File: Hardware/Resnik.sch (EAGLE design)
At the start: 212 parts, among them IC1 ATMEGA1284M, J1 CONN_82.54_SCREW, J3 CONN_42.54_SCREW, J4 CONN_82.54_SCREW, Q1 DMG3404, Q2 DMG3404, Q3 FDN360P, Q4 2N7002, Q5 FDN360P, Q6 DMG3404, Q7 2N7002, Q8 2N7002, U1 TLV61220DBV, U10 TPS22917DBV, U11 SN74AUP1G04YFP, U12 SN74AUP1G04YFP, U13 SN74AUP1G04YFP, U14 SN74AUP2G08DQE, U15 SN74AUP2G08DQE, U16 SN74AUP2G08DQE, U17 MIC2544MSOP, U18 MIC2544MSOP, U19 MIC2544MSOP, U2 TPS62822DLC, U20 MIC2544MSOP, U21 TPS22917DBV, U22 TPS22917DBV, U23 FT231X-Q, U24 SN74LVC1G3157DRL, U25 SN74AUP3G34DCU, U26 TXS0102DQM, U27 TXS0104RGY, U28 TCA9406DCU, U29 TXS0104RGY, U3 TPS61032RSA, U30 MCP4726A2SOT-23, U31 BME280, U32 ADS1115, U33 ADS1115, U34 INA211DCK, U35 INA213DCK, U36 TCA9406DCU, U37 TLV3691DCK, U38 TS5A21366RSE, U39 MIC94094C6, U40 SN74AHC1G86DCK, U41 MCP23018QFN, U42 TXS0104RGY, U5 BQ2980RUG, U6 TPS2105, U7 LTC4412S6, U8 TPL5111DDC, U9 TPS79733

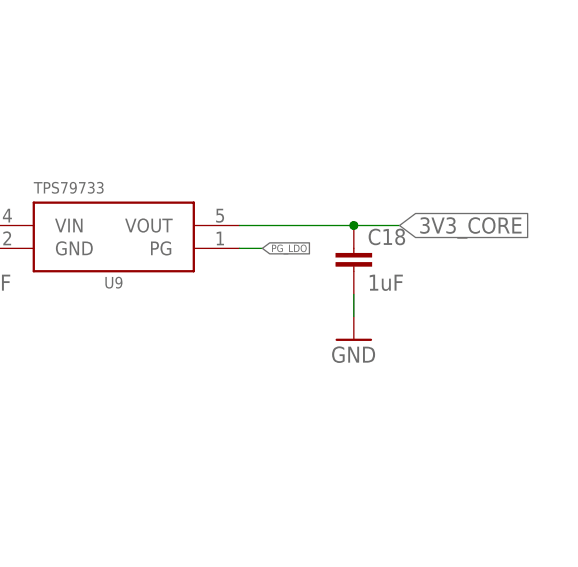
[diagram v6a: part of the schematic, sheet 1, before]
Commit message: Added Ref ID images, updated BoM for new parts, added pick and place
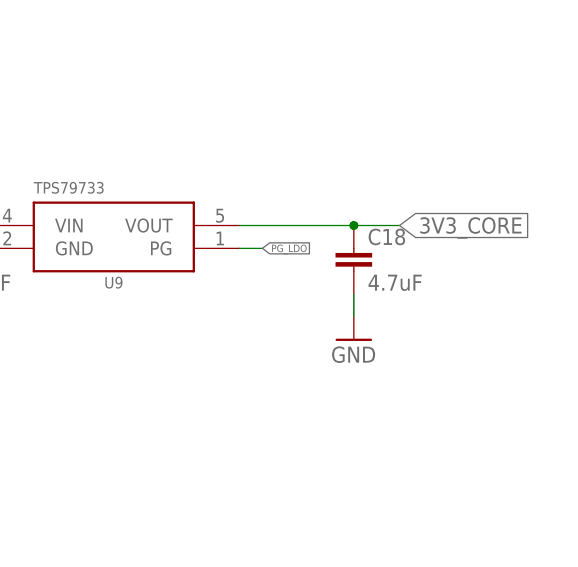
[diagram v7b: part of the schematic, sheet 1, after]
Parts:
- C18: value 1uF -> 4.7uF; device bschulz_passives:C-EU1UFC0603 -> bschulz_passives:C-EU4.7UFC0603
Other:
- note added: "J8"
- note added: "J9"
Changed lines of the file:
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@@
 <?xml version="1.0" encoding="utf-8"?>
 <!DOCTYPE eagle SYSTEM "eagle.dtd">
-<eagle version="9.2.1">
+<eagle version="9.4.2">
 <drawing>
 <settings>
@@
 <grid distance="0.1" unitdist="inch" unit="inch" style="lines" multiple="1" display="no" altdistance="0.01" altunitdist="inch" altunit="inch"/>
 <layers>
-<layer number="1" name="Top" color="4" fill="1" visible="yes" active="no"/>
-<layer number="2" name="Route2" color="16" fill="1" visible="yes" active="no"/>
-<layer number="3" name="Route3" color="17" fill="1" visible="yes" active="no"/>
-<layer number="4" name="Route4" color="18" fill="1" visible="yes" active="no"/>
-<layer number="5" name="Route5" color="19" fill="1" visible="yes" active="no"/>
-<layer number="6" name="Route6" color="25" fill="1" visible="yes" active="no"/>
-<layer number="7" name="Route7" color="26" fill="1" visible="yes" active="no"/>
-<layer number="8" name="Route8" color="27" fill="1" visible="yes" active="no"/>
-<layer number="9" name="Route9" color="28" fill="1" visible="yes" active="no"/>
-<layer number="10" name="Route10" color="29" fill="1" visible="yes" active="no"/>
-<layer number="11" name="Route11" color="30" fill="1" visible="yes" active="no"/>
-<layer number="12" name="Route12" color="20" fill="1" visible="yes" active="no"/>
-<layer number="13" name="Route13" color="21" fill="1" visible="yes" active="no"/>
-<layer number="14" name="Route14" color="22" fill="1" visible="yes" active="no"/>
-<layer number="15" name="Route15" color="23" fill="1" visible="yes" active="no"/>
-<layer number="16" name="Bottom" color="1" fill="1" visible="yes" active="no"/>
-<layer number="17" name="Pads" color="2" fill="1" visible="yes" active="no"/>
-<layer number="18" name="Vias" color="2" fill="1" visible="yes" active="no"/>
-<layer number="19" name="Unrouted" color="6" fill="1" visible="yes" active="no"/>
-<layer number="20" name="Dimension" color="24" fill="1" visible="yes" active="no"/>
-<layer number="21" name="tPlace" color="7" fill="1" visible="yes" active="no"/>
-<layer number="22" name="bPlace" color="7" fill="1" visible="yes" active="no"/>
-<layer number="23" name="tOrigins" color="15" fill="1" visible="yes" active="no"/>
-<layer number="24" name="bOrigins" color="15" fill="1" visible="yes" active="no"/>
-<layer number="25" name="tNames" color="7" fill="1" visible="yes" active="no"/>
-<layer number="26" name="bNames" color="7" fill="1" visible="yes" active="no"/>
-<layer number="27" name="tValues" color="7" fill="1" visible="yes" active="no"/>
-<layer number="28" name="bValues" color="7" fill="1" visible="yes" active="no"/>
+<layer number="1" name="Top" color="4" fill="1" visible="no" active="no"/>
+<layer number="2" name="Route2" color="16" fill="1" visible="no" active="no"/>
+<layer number="3" name="Route3" color="17" fill="1" visible="no" active="no"/>
+<layer number="4" name="Route4" color="18" fill="1" visible="no" active="no"/>
+<layer number="5" name="Route5" color="19" fill="1" visible="no" active="no"/>
+<layer number="6" name="Route6" color="25" fill="1" visible="no" active="no"/>
+<layer number="7" name="Route7" color="26" fill="1" visible="no" active="no"/>
+<layer number="8" name="Route8" color="27" fill="1" visible="no" active="no"/>
+<layer number="9" name="Route9" color="28" fill="1" visible="no" active="no"/>
+<layer number="10" name="Route10" color="29" fill="1" visible="no" active="no"/>
+<layer number="11" name="Route11" color="30" fill="1" visible="no" active="no"/>
+<layer number="12" name="Route12" color="20" fill="1" visible="no" active="no"/>
+<layer number="13" name="Route13" color="21" fill="1" visible="no" active="no"/>
+<layer number="14" name="Route14" color="22" fill="1" visible="no" active="no"/>
+<layer number="15" name="Route15" color="23" fill="1" visible="no" active="no"/>
+<layer number="16" name="Bottom" color="1" fill="1" visible="no" active="no"/>
+<layer number="17" name="Pads" color="2" fill="1" visible="no" active="no"/>
+<layer number="18" name="Vias" color="2" fill="1" visible="no" active="no"/>
+<layer number="19" name="Unrouted" color="6" fill="1" visible="no" active="no"/>
+<layer number="20" name="Dimension" color="24" fill="1" visible="no" active="no"/>
+<layer number="21" name="tPlace" color="7" fill="1" visible="no" active="no"/>
+<layer number="22" name="bPlace" color="7" fill="1" visible="no" active="no"/>
+<layer number="23" name="tOrigins" color="15" fill="1" visible="no" active="no"/>
+<layer number="24" name="bOrigins" color="15" fill="1" visible="no" active="no"/>
+<layer number="25" name="tNames" color="7" fill="1" visible="no" active="no"/>
+<layer number="26" name="bNames" color="7" fill="1" visible="no" active="no"/>
+<layer number="27" name="tValues" color="7" fill="1" visible="no" active="no"/>
+<layer number="28" name="bValues" color="7" fill="1" visible="no" active="no"/>
 <layer number="29" name="tStop" color="7" fill="3" visible="no" active="no"/>
 <layer number="30" name="bStop" color="7" fill="6" visible="no" active="no"/>
@@
 <layer number="35" name="tGlue" color="7" fill="4" visible="no" active="no"/>
 <layer number="36" name="bGlue" color="7" fill="5" visible="no" active="no"/>
-<layer number="37" name="tTest" color="7" fill="1" visible="yes" active="no"/>
-<layer number="38" name="bTest" color="7" fill="1" visible="yes" active="no"/>
+<layer number="37" name="tTest" color="7" fill="1" visible="no" active="no"/>
+<layer number="38" name="bTest" color="7" fill="1" visible="no" active="no"/>
 <layer number="39" name="tKeepout" color="4" fill="11" visible="no" active="no"/>
 <layer number="40" name="bKeepout" color="1" fill="11" visible="no" active="no"/>
@@
 <layer number="44" name="Drills" color="7" fill="1" visible="no" active="no"/>
 <layer number="45" name="Holes" color="7" fill="1" visible="no" active="no"/>
-<layer number="46" name="Milling" color="3" fill="1" visible="yes" active="no"/>
-<layer number="47" name="Measures" color="7" fill="1" visible="yes" active="no"/>
-<layer number="48" name="Document" color="7" fill="1" visible="yes" active="no"/>
-<layer number="49" name="Reference" color="7" fill="1" visible="yes" active="no"/>
-<layer number="50" name="dxf" color="7" fill="1" visible="yes" active="no"/>
-<layer number="51" name="tDocu" color="7" fill="1" visible="yes" active="no"/>
-<layer number="52" name="bDocu" color="7" fill="1" visible="yes" active="no"/>
-<layer number="53" name="tGND_GNDA" color="7" fill="1" visible="yes" active="no"/>
-<layer number="54" name="bGND_GNDA" color="7" fill="1" visible="yes" active="no"/>
-<layer number="56" name="wert" color="7" fill="1" visible="yes" active="no"/>
-<layer number="57" name="tCAD" color="7" fill="1" visible="yes" active="no"/>
-<layer number="59" name="tCarbon" color="7" fill="1" visible="yes" active="no"/>
-<layer number="60" name="bCarbon" color="7" fill="1" visible="yes" active="no"/>
+<layer number="46" name="Milling" color="3" fill="1" visible="no" active="no"/>
+<layer number="47" name="Measures" color="7" fill="1" visible="no" active="no"/>
+<layer number="48" name="Document" color="7" fill="1" visible="no" active="no"/>
+<layer number="49" name="Reference" color="7" fill="1" visible="no" active="no"/>
+<layer number="50" name="dxf" color="7" fill="1" visible="no" active="no"/>
+<layer number="51" name="tDocu" color="7" fill="1" visible="no" active="no"/>
+<layer number="52" name="bDocu" color="7" fill="1" visible="no" active="no"/>
+<layer number="53" name="tGND_GNDA" color="7" fill="1" visible="no" active="no"/>
+<layer number="54" name="bGND_GNDA" color="7" fill="1" visible="no" active="no"/>
+<layer number="56" name="wert" color="7" fill="1" visible="no" active="no"/>
+<layer number="57" name="tCAD" color="7" fill="1" visible="no" active="no"/>
+<layer number="59" name="tCarbon" color="7" fill="1" visible="no" active="no"/>
+<layer number="60" name="bCarbon" color="7" fill="1" visible="no" active="no"/>
 <layer number="88" name="SimResults" color="9" fill="1" visible="yes" active="yes"/>
 <layer number="89" name="SimProbes" color="9" fill="1" visible="yes" active="yes"/>
@@
 <part name="C17" library="bschulz_passives" deviceset="C-EU" device="C0402" technology="0.1UF" value="0.1uF"/>
 <part name="GND26" library="supply1" library_urn="urn:adsk.eagle:library:371" deviceset="GND" device=""/>
-<part name="C18" library="bschulz_passives" deviceset="C-EU" device="C0603" technology="1UF" value="1uF"/>
+<part name="C18" library="bschulz_passives" deviceset="C-EU" device="C0603" technology="4.7UF" value="4.7uF"/>
 <part name="GND27" library="supply1" library_urn="urn:adsk.eagle:library:371" deviceset="GND" device=""/>
 <part name="U7" library="bschulz" deviceset="LTC4412" device="S6"/>
@@
 <text x="129.54" y="91.44" size="1.778" layer="91">ICSP</text>
 <text x="134.62" y="114.3" size="1.778" layer="91">Jump SDA channels together, prevents using occupied addresses on the external I2C port</text>
+<text x="111.76" y="66.04" size="1.778" layer="95">J8</text>
+<text x="152.4" y="66.04" size="1.778" layer="95">J9</text>
 </plain>
 <instances>

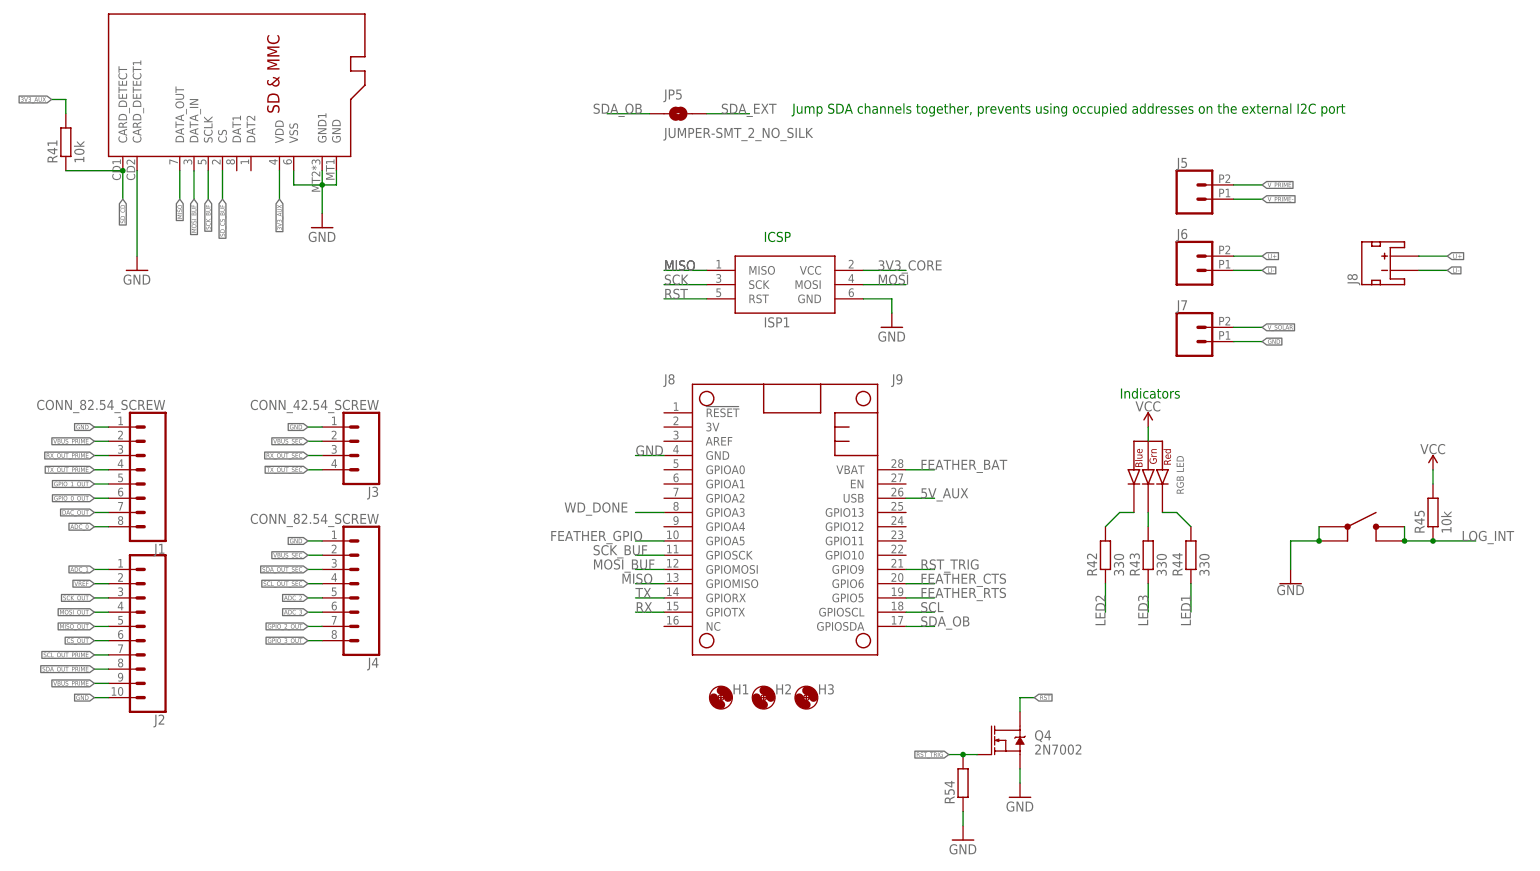
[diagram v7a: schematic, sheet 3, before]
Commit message: Added reference designators, cleanup
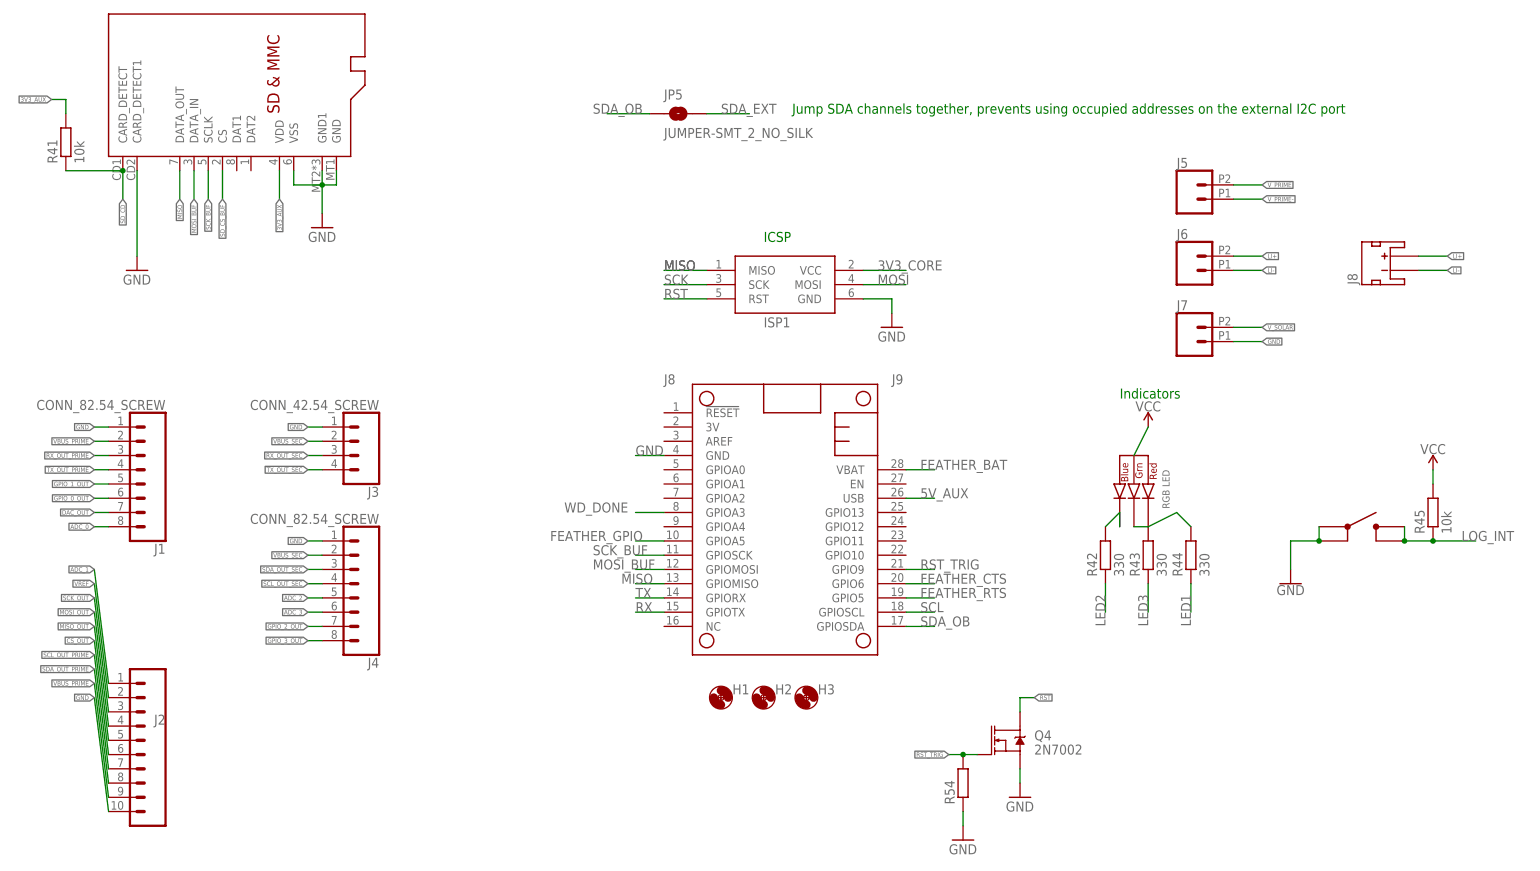
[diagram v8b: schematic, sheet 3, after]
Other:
- moved on the sheet: J2
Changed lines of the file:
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@@
 <wire x1="299.212" y1="109.22" x2="284.48" y2="109.22" width="0.1524" layer="91"/>
 <pinref part="D4" gate="G$1" pin="ANODE"/>
-<wire x1="299.212" y1="112.014" x2="299.212" y2="109.22" width="0.1524" layer="91"/>
+<wire x1="296.672" y1="114.554" x2="299.212" y2="109.22" width="0.1524" layer="91"/>
 <label x="284.48" y="109.22" size="1.778" layer="95" rot="R180" xref="yes"/>
 </segment>
@@
 <pinref part="D4" gate="G$1" pin="RED_CATH"/>
 <wire x1="307.086" y1="126.492" x2="307.086" y2="124.714" width="0.1524" layer="91"/>
-<wire x1="307.086" y1="124.714" x2="301.752" y2="124.714" width="0.1524" layer="91"/>
+<wire x1="307.086" y1="124.714" x2="299.212" y2="127.254" width="0.1524" layer="91"/>
 </segment>
 </net>
@@
 <pinref part="D4" gate="G$1" pin="BLUE_CATH"/>
 <pinref part="R36" gate="G$1" pin="1"/>
-<wire x1="296.672" y1="124.714" x2="292.1" y2="124.714" width="0.1524" layer="91"/>
+<wire x1="294.132" y1="127.254" x2="292.1" y2="124.714" width="0.1524" layer="91"/>
 <wire x1="292.1" y1="124.714" x2="292.1" y2="127" width="0.1524" layer="91"/>
 </segment>
@@
 <pinref part="D4" gate="G$1" pin="GREEN_CATH"/>
 <pinref part="R37" gate="G$1" pin="1"/>
-<wire x1="299.212" y1="124.714" x2="299.212" y2="126.492" width="0.1524" layer="91"/>
+<wire x1="296.672" y1="127.254" x2="299.212" y2="126.492" width="0.1524" layer="91"/>
 </segment>
 </net>
@@
 <pinref part="D5" gate="G$1" pin="BLUE_CATH"/>
 <wire x1="190.5" y1="40.64" x2="193.04" y2="43.18" width="0.1524" layer="91"/>
-<wire x1="193.04" y1="43.18" x2="195.58" y2="43.18" width="0.1524" layer="91"/>
+<wire x1="193.04" y1="43.18" x2="193.04" y2="40.64" width="0.1524" layer="91"/>
 </segment>
 </net>
@@
 <pinref part="R43" gate="G$1" pin="2"/>
 <pinref part="D5" gate="G$1" pin="GREEN_CATH"/>
-<wire x1="198.12" y1="40.64" x2="198.12" y2="43.18" width="0.1524" layer="91"/>
+<wire x1="198.12" y1="40.64" x2="195.58" y2="40.64" width="0.1524" layer="91"/>
 </segment>
 </net>
@@
 <pinref part="D5" gate="G$1" pin="RED_CATH"/>
 <pinref part="R44" gate="G$1" pin="2"/>
-<wire x1="200.66" y1="43.18" x2="203.2" y2="43.18" width="0.1524" layer="91"/>
+<wire x1="198.12" y1="40.64" x2="203.2" y2="43.18" width="0.1524" layer="91"/>
 <wire x1="203.2" y1="43.18" x2="205.74" y2="40.64" width="0.1524" layer="91"/>
 </segment>
@@
 <segment>
 <pinref part="J2" gate="G$1" pin="10"/>
-<wire x1="12.7" y1="10.16" x2="10.16" y2="10.16" width="0.1524" layer="91"/>
+<wire x1="12.7" y1="-10.16" x2="10.16" y2="10.16" width="0.1524" layer="91"/>
 <label x="10.16" y="10.16" size="0.8128" layer="95" rot="R180" xref="yes"/>
 </segment>
@@
 <pinref part="SUPPLY9" gate="G$1" pin="VCC"/>
 <pinref part="D5" gate="G$1" pin="ANODE"/>
-<wire x1="198.12" y1="58.42" x2="198.12" y2="55.88" width="0.1524" layer="91"/>
+<wire x1="198.12" y1="58.42" x2="195.58" y2="53.34" width="0.1524" layer="91"/>
 </segment>
 <segment>
@@
 <segment>
 <pinref part="J2" gate="G$1" pin="1"/>
-<wire x1="12.7" y1="33.02" x2="10.16" y2="33.02" width="0.1524" layer="91"/>
+<wire x1="12.7" y1="12.7" x2="10.16" y2="33.02" width="0.1524" layer="91"/>
 <label x="10.16" y="33.02" size="0.8128" layer="95" rot="R180" xref="yes"/>
 </segment>
@@
 <segment>
 <pinref part="J2" gate="G$1" pin="2"/>
-<wire x1="12.7" y1="30.48" x2="10.16" y2="30.48" width="0.1524" layer="91"/>
+<wire x1="12.7" y1="10.16" x2="10.16" y2="30.48" width="0.1524" layer="91"/>
 <label x="10.16" y="30.48" size="0.8128" layer="95" rot="R180" xref="yes"/>
 </segment>
@@
 <segment>
 <pinref part="J2" gate="G$1" pin="3"/>
-<wire x1="12.7" y1="27.94" x2="10.16" y2="27.94" width="0.1524" layer="91"/>
+<wire x1="12.7" y1="7.62" x2="10.16" y2="27.94" width="0.1524" layer="91"/>
 <label x="10.16" y="27.94" size="0.8128" layer="95" rot="R180" xref="yes"/>
 </segment>
@@
 <segment>
 <pinref part="J2" gate="G$1" pin="6"/>
-<wire x1="12.7" y1="20.32" x2="10.16" y2="20.32" width="0.1524" layer="91"/>
+<wire x1="12.7" y1="0" x2="10.16" y2="20.32" width="0.1524" layer="91"/>
 <label x="10.16" y="20.32" size="0.8128" layer="95" rot="R180" xref="yes"/>
 </segment>
@@
 <segment>
 <pinref part="J2" gate="G$1" pin="7"/>
-<wire x1="12.7" y1="17.78" x2="10.16" y2="17.78" width="0.1524" layer="91"/>
+<wire x1="12.7" y1="-2.54" x2="10.16" y2="17.78" width="0.1524" layer="91"/>
 <label x="10.16" y="17.78" size="0.8128" layer="95" rot="R180" xref="yes"/>
 </segment>
@@
 <segment>
 <pinref part="J2" gate="G$1" pin="8"/>
-<wire x1="12.7" y1="15.24" x2="10.16" y2="15.24" width="0.1524" layer="91"/>
+<wire x1="12.7" y1="-5.08" x2="10.16" y2="15.24" width="0.1524" layer="91"/>
 <label x="10.16" y="15.24" size="0.8128" layer="95" rot="R180" xref="yes"/>
 </segment>
@@
 <segment>
 <pinref part="J2" gate="G$1" pin="9"/>
-<wire x1="12.7" y1="12.7" x2="10.16" y2="12.7" width="0.1524" layer="91"/>
+<wire x1="12.7" y1="-7.62" x2="10.16" y2="12.7" width="0.1524" layer="91"/>
 <label x="10.16" y="12.7" size="0.8128" layer="95" rot="R180" xref="yes"/>
 </segment>
@@
 <segment>
 <pinref part="J2" gate="G$1" pin="4"/>
-<wire x1="12.7" y1="25.4" x2="10.16" y2="25.4" width="0.1524" layer="91"/>
+<wire x1="12.7" y1="5.08" x2="10.16" y2="25.4" width="0.1524" layer="91"/>
 <label x="10.16" y="25.4" size="0.8128" layer="95" rot="R180" xref="yes"/>
 </segment>
@@
 <segment>
 <pinref part="J2" gate="G$1" pin="5"/>
-<wire x1="12.7" y1="22.86" x2="10.16" y2="22.86" width="0.1524" layer="91"/>
+<wire x1="12.7" y1="2.54" x2="10.16" y2="22.86" width="0.1524" layer="91"/>
 <label x="10.16" y="22.86" size="0.8128" layer="95" rot="R180" xref="yes"/>
 </segment>
